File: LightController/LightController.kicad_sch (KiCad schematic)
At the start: 6 parts, among them J1 Conn_01x04_Male, U1 mh-et-live-minikit, U2 TLC59208F, U3 TLC59208F, U4 TLC59208F, U5 TLC59208F

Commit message: routing almost done
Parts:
- removed J1: Conn_01x04_Male, Connector_Phoenix_MC:PhoenixContact_MCV_1,5_4-G-3.5_1x04_P3.50mm_Vertical, symbol Connector:Conn_01x04_Male
- removed U2, U3, U4, U5: TLC59208F, Package_SO:TSSOP-16_4.4x5mm_P0.65mm, symbol bouni:TLC59208F
- added BTN1, BTN2: SW_Push_Open, Button_Switch_SMD:SW_SPST_Omron_B3FS-101xP, symbol Switch:SW_Push_Open
- added D1, D2, D3, D4, D5, D6: LED, LED_SMD:LED_0603_1608Metric, symbol Device:LED
- added F1: Fuse, Fuse:Fuseholder_Cylinder-5x20mm_Schurter_0031_8201_Horizontal_Open, symbol Device:Fuse
- added J0, J1, J2, J3, J4, J5, J6, J7: Conn_01x08_Female, bouni:SPTAF_1_8_3_5_EL, symbol Connector:Conn_01x08_Female
- added J8: Conn_01x02_Female, Connector_Phoenix_MC:PhoenixContact_MC_1,5_2-G-3.5_1x02_P3.50mm_Horizontal, symbol Connector:Conn_01x02_Female
- added JP1: Jumper_2_Open, Jumper:SolderJumper-2_P1.3mm_Open_RoundedPad1.0x1.5mm, symbol Jumper:Jumper_2_Open
- added Q0, Q1, Q10, Q11, Q12, Q13, Q14, Q15, Q16, Q17, Q18, Q19, Q2, Q20, Q21, Q22, Q23, Q24, Q25, Q26, Q27, Q28, Q29, Q3, Q30, Q31, Q32, Q33, Q34, Q35, Q4, Q5, Q6, Q7, Q8, Q9: IRLML0030, Package_TO_SOT_SMD:SOT-23, symbol Transistor_FET:IRLML0030
- added R1: 10K, Resistor_SMD:R_0603_1608Metric, symbol Device:R
- added R2, R3, R4, R5, R6, R7: R, Resistor_SMD:R_0603_1608Metric, symbol Device:R
- added RN1, RN2, RN3, RN4, RN5, RN6, RN7, RN8, RN9: 10k, Resistor_SMD:R_Array_Concave_4x0603, symbol Device:R_Pack04_Split
- added U2, U3: MCP23017_SO, Package_SO:SSOP-28_5.3x10.2mm_P0.65mm, symbol Interface_Expansion:MCP23017_SO
- added U4: D-SUN-MP1584EN, bouni:D-SUN-MP1584EN, symbol bouni:D-SUN-MP1584EN
- added U5: DHT22, Sensor:Aosong_DHT11_5.5x12.0_P2.54mm, symbol Sensor:DHT11
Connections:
- net 5V is gone; now on net +5V: U1.28 (5V)
- net +5V: now also R1.1, R3.2, R4.2, R5.2, R6.2, R7.2, U2.10 (VSS), U3.10 (VSS), U3.15 (A0), U4.7 (VOUT+), U4.8 (VOUT+)
- net GND: now also BTN1.1 (A), BTN2.1 (A), D1.1 (K), D4.1 (K), J8.2 (Pin_2), Q0.3 (D), Q1.3 (D), Q10.3 (D), Q11.3 (D), Q12.3 (D), Q13.3 (D), Q14.3 (D), Q15.3 (D), Q16.3 (D), Q17.3 (D), Q18.3 (D), Q19.3 (D), Q2.3 (D), Q20.3 (D), Q21.3 (D), Q22.3 (D), Q23.3 (D), Q24.3 (D), Q25.3 (D), Q26.3 (D), Q27.3 (D), Q28.3 (D), Q29.3 (D), Q3.3 (D), Q30.3 (D), Q31.3 (D), Q32.3 (D), Q33.3 (D), Q34.3 (D), Q35.3 (D), Q4.3 (D), Q5.3 (D), Q6.3 (D), Q7.3 (D), Q8.3 (D), Q9.3 (D), RN1.5 (R4.2), RN1.6 (R3.2), RN1.7 (R2.2), RN1.8 (R1.2), RN2.5 (R4.2), RN2.6 (R3.2), RN2.7 (R2.2), RN2.8 (R1.2), RN3.5 (R4.2), RN3.6 (R3.2), RN3.7 (R2.2), RN3.8 (R1.2), RN4.5 (R4.2), RN4.6 (R3.2), RN4.7 (R2.2), RN4.8 (R1.2), RN5.5 (R4.2), RN5.6 (R3.2), RN5.7 (R2.2), RN5.8 (R1.2), RN6.5 (R4.2), RN6.6 (R3.2), RN6.7 (R2.2), RN6.8 (R1.2), RN7.5 (R4.2), RN7.6 (R3.2), RN7.7 (R2.2), RN7.8 (R1.2), RN8.5 (R4.2), RN8.6 (R3.2), RN8.7 (R2.2), RN8.8 (R1.2), RN9.5 (R4.2), RN9.6 (R3.2), RN9.7 (R2.2), RN9.8 (R1.2), U2.15 (A0), U2.16 (A1), U2.17 (A2), U2.9 (VDD), U3.16 (A1), U3.17 (A2), U3.9 (VDD), U4.1 (VIN-), U4.2 (VIN-), U4.5 (VOUT-), U4.6 (VOUT-), U5.4 (GND)
- net RESET: now also JP1.1 (A), R1.2, U2.18 (~RESET~), U3.18 (~RESET~)
- net SCL: now also U2.12 (SCK), U3.12 (SCK)
- net SDA: now also U2.13 (SDA), U3.13 (SDA)
- net at U1.11 (RST): now also JP1.2 (B)
- net +3V3: now reaches U1.18 (3V3)
- net +3V3: now also U5.1 (VCC)
- net BTN1: now reaches U1.25 (IO17)
- net BTN1: now also BTN1.2 (B)
- net BTN2: now reaches U1.26 (IO16)
- net BTN2: now also BTN2.2 (B)
- net DHT22: now reaches U1.32 (IO27)
- net DHT22: now also U5.2 (IO)
- net LED1: now reaches U1.33 (IO25)
- net LED1: now also Q32.1 (G), RN9.1 (R1.1)
- net LED2: now reaches U1.34 (IO32)
- net LED2: now also Q33.1 (G), RN9.2 (R2.1)
- net LED3: now reaches U1.35 (TDI)
- net LED3: now also Q34.1 (G), RN9.3 (R3.1)
- net LED4: now reaches U1.36 (IO4)
- net LED4: now also Q35.1 (G), RN9.4 (R4.1)
- new net: D2.1 (K), Q32.2 (S)
- new net: D6.1 (K), Q35.2 (S)
- new net: D6.2 (A), R7.1
- new net: D3.1 (K), Q33.2 (S)
- new net: F1.2, J8.1 (Pin_1)
- new net: D2.2 (A), R3.1
- new net: D3.2 (A), R4.1
- new net: D5.2 (A), R6.1
- new net: D1.2 (A), R2.1
- new net: D4.2 (A), R5.1
- new net: D5.1 (K), Q34.2 (S)
- new net +12V: F1.1, J0.1 (Pin_1), J0.3 (Pin_3), J0.5 (Pin_5), J0.7 (Pin_7), J1.1 (Pin_1), J1.3 (Pin_3), J1.5 (Pin_5), J1.7 (Pin_7), J2.1 (Pin_1), J2.3 (Pin_3), J2.5 (Pin_5), J2.7 (Pin_7), J3.1 (Pin_1), J3.3 (Pin_3), J3.5 (Pin_5), J3.7 (Pin_7), J4.1 (Pin_1), J4.3 (Pin_3), J4.5 (Pin_5), J4.7 (Pin_7), J5.1 (Pin_1), J5.3 (Pin_3), J5.5 (Pin_5), J5.7 (Pin_7), J6.1 (Pin_1), J6.3 (Pin_3), J6.5 (Pin_5), J6.7 (Pin_7), J7.1 (Pin_1), J7.3 (Pin_3), J7.5 (Pin_5), J7.7 (Pin_7), R2.2, U4.3 (VIN+), U4.4 (VIN+)
- new net GPIO0: Q0.1 (G), RN1.1 (R1.1), U2.21 (GPA0)
- new net GPIO1: Q1.1 (G), RN1.2 (R2.1), U2.22 (GPA1)
- new net GPIO10: Q10.1 (G), RN3.3 (R3.1), U2.3 (GPB2)
- new net GPIO11: Q11.1 (G), RN3.4 (R4.1), U2.4 (GPB3)
- new net GPIO12: Q12.1 (G), RN4.1 (R1.1), U2.5 (GPB4)
- new net GPIO13: Q13.1 (G), RN4.2 (R2.1), U2.6 (GPB5)
- new net GPIO14: Q14.1 (G), RN4.3 (R3.1), U2.7 (GPB6)
- new net GPIO15: Q15.1 (G), RN4.4 (R4.1), U2.8 (GPB7)
- new net GPIO16: Q16.1 (G), RN5.1 (R1.1), U3.21 (GPA0)
- new net GPIO17: Q17.1 (G), RN5.2 (R2.1), U3.22 (GPA1)
- new net GPIO18: Q18.1 (G), RN5.3 (R3.1), U3.23 (GPA2)
- new net GPIO19: Q19.1 (G), RN5.4 (R4.1), U3.24 (GPA3)
- new net GPIO2: Q2.1 (G), RN1.3 (R3.1), U2.23 (GPA2)
- new net GPIO20: Q20.1 (G), RN6.1 (R1.1), U3.25 (GPA4)
- new net GPIO21: Q21.1 (G), RN6.2 (R2.1), U3.26 (GPA5)
- new net GPIO22: Q22.1 (G), RN6.3 (R3.1), U3.27 (GPA6)
- new net GPIO23: Q23.1 (G), RN6.4 (R4.1), U3.28 (GPA7)
- new net GPIO24: Q24.1 (G), RN7.1 (R1.1), U3.1 (GPB0)
- new net GPIO25: Q25.1 (G), RN7.2 (R2.1), U3.2 (GPB1)
- new net GPIO26: Q26.1 (G), RN7.3 (R3.1), U3.3 (GPB2)
- new net GPIO27: Q27.1 (G), RN7.4 (R4.1), U3.4 (GPB3)
- new net GPIO28: Q28.1 (G), RN8.1 (R1.1), U3.5 (GPB4)
- new net GPIO29: Q29.1 (G), RN8.2 (R2.1), U3.6 (GPB5)
- new net GPIO3: Q3.1 (G), RN1.4 (R4.1), U2.24 (GPA3)
- new net GPIO30: Q30.1 (G), RN8.3 (R3.1), U3.7 (GPB6)
- new net GPIO31: Q31.1 (G), RN8.4 (R4.1), U3.8 (GPB7)
- new net GPIO4: Q4.1 (G), RN2.1 (R1.1), U2.25 (GPA4)
- new net GPIO5: Q5.1 (G), RN2.2 (R2.1), U2.26 (GPA5)
- new net GPIO6: Q6.1 (G), RN2.3 (R3.1), U2.27 (GPA6)
- new net GPIO7: Q7.1 (G), RN2.4 (R4.1), U2.28 (GPA7)
- new net GPIO8: Q8.1 (G), RN3.1 (R1.1), U2.1 (GPB0)
- new net GPIO9: Q9.1 (G), RN3.2 (R2.1), U2.2 (GPB1)
- new net OUT0: J0.2 (Pin_2), Q0.2 (S)
- new net OUT1: J0.4 (Pin_4), Q1.2 (S)
- new net OUT10: J2.6 (Pin_6), Q10.2 (S)
- new net OUT11: J2.8 (Pin_8), Q11.2 (S)
- new net OUT12: J3.2 (Pin_2), Q12.2 (S)
- new net OUT13: J3.4 (Pin_4), Q13.2 (S)
- new net OUT14: J3.6 (Pin_6), Q14.2 (S)
- new net OUT15: J3.8 (Pin_8), Q15.2 (S)
- new net OUT16: J4.2 (Pin_2), Q16.2 (S)
- new net OUT17: J4.4 (Pin_4), Q17.2 (S)
- new net OUT18: J4.6 (Pin_6), Q18.2 (S)
- new net OUT19: J4.8 (Pin_8), Q19.2 (S)
- new net OUT2: J0.6 (Pin_6), Q2.2 (S)
- new net OUT20: J5.2 (Pin_2), Q20.2 (S)
- new net OUT21: J5.4 (Pin_4), Q21.2 (S)
- new net OUT22: J5.6 (Pin_6), Q22.2 (S)
- new net OUT23: J5.8 (Pin_8), Q23.2 (S)
- new net OUT24: J6.2 (Pin_2), Q24.2 (S)
- new net OUT25: J6.4 (Pin_4), Q25.2 (S)
- new net OUT26: J6.6 (Pin_6), Q26.2 (S)
- new net OUT27: J6.8 (Pin_8), Q27.2 (S)
- new net OUT28: J7.2 (Pin_2), Q28.2 (S)
- new net OUT29: J7.4 (Pin_4), Q29.2 (S)
- new net OUT3: J0.8 (Pin_8), Q3.2 (S)
- new net OUT30: J7.6 (Pin_6), Q30.2 (S)
- new net OUT31: J7.8 (Pin_8), Q31.2 (S)
- new net OUT4: J1.2 (Pin_2), Q4.2 (S)
- new net OUT5: J1.4 (Pin_4), Q5.2 (S)
- new net OUT6: J1.6 (Pin_6), Q6.2 (S)
- new net OUT7: J1.8 (Pin_8), Q7.2 (S)
- new net OUT8: J2.2 (Pin_2), Q8.2 (S)
- new net OUT9: J2.4 (Pin_4), Q9.2 (S)
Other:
- note added: "Connectors: SPTAF 1/ 8-3,5-EL - 1862107"
- note removed: "40h"
- note removed: "42h"
- note removed: "44h"
- note removed: "46h"
- moved on the sheet: U1

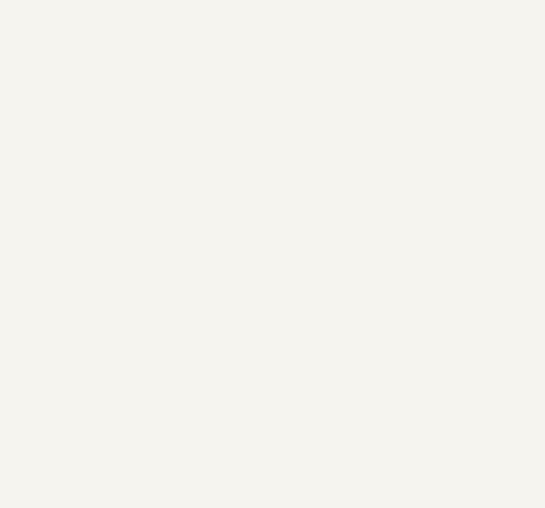
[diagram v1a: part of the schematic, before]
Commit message: made pcb slightly bigger for mounting holes
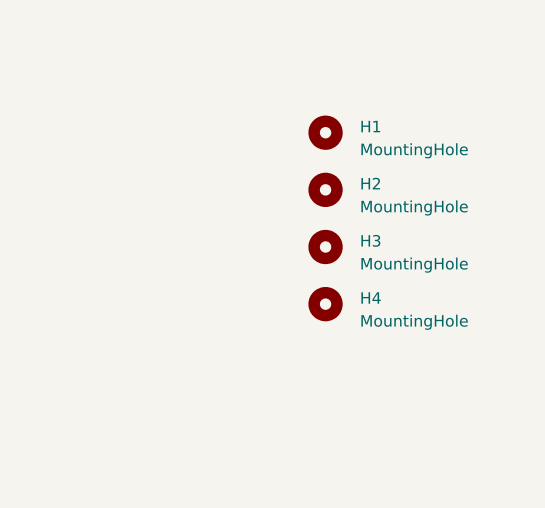
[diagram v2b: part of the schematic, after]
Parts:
- added H1, H2, H3, H4: MountingHole, MountingHole:MountingHole_3.2mm_M3, symbol Mechanical:MountingHole
- J8: footprint Connector_Phoenix_MC:PhoenixContact_MC_1,5_2-G-3.5_1x02_P3.50mm_Horizontal -> bouni:SPTAF_1_2_3_5_EL
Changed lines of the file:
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@@
     (pin "1")
+  )
+  (symbol (lib_id "Mechanical:MountingHole") (at 381 25.4 0) (unit 1)
+    (in_bom yes) (on_board yes)
+    (property "Reference" "H1" (id 0) (at 384.81 24.7649 0)
+      (effects (font (size 1.27 1.27)) (justify left))
+    )
+    (property "Value" "MountingHole" (id 1) (at 384.81 27.3049 0)
+      (effects (font (size 1.27 1.27)) (justify left))
+    )
+    (property "Footprint" "MountingHole:MountingHole_3.2mm_M3" (id 2) (at 381 25.4 0)
+      (effects (font (size 1.27 1.27)) hide)
+    )
+    (property "Datasheet" "~" (id 3) (at 381 25.4 0)
+      (effects (font (size 1.27 1.27)) hide)
+    )
+  )
+  (symbol (lib_id "Mechanical:MountingHole") (at 381 31.75 0) (unit 1)
+    (in_bom yes) (on_board yes)
+    (property "Reference" "H2" (id 0) (at 384.81 31.1149 0)
+      (effects (font (size 1.27 1.27)) (justify left))
+    )
+    (property "Value" "MountingHole" (id 1) (at 384.81 33.6549 0)
+      (effects (font (size 1.27 1.27)) (justify left))
+    )
+    (property "Footprint" "MountingHole:MountingHole_3.2mm_M3" (id 2) (at 381 31.75 0)
+      (effects (font (size 1.27 1.27)) hide)
+    )
+    (property "Datasheet" "~" (id 3) (at 381 31.75 0)
+      (effects (font (size 1.27 1.27)) hide)
+    )
+  )
+  (symbol (lib_id "Mechanical:MountingHole") (at 381 38.1 0) (unit 1)
+    (in_bom yes) (on_board yes)
+    (property "Reference" "H3" (id 0) (at 384.81 37.4649 0)
+      (effects (font (size 1.27 1.27)) (justify left))
+    )
+    (property "Value" "MountingHole" (id 1) (at 384.81 40.0049 0)
+      (effects (font (size 1.27 1.27)) (justify left))
+    )
+    (property "Footprint" "MountingHole:MountingHole_3.2mm_M3" (id 2) (at 381 38.1 0)
+      (effects (font (size 1.27 1.27)) hide)
+    )
+    (property "Datasheet" "~" (id 3) (at 381 38.1 0)
+      (effects (font (size 1.27 1.27)) hide)
+    )
+  )
+  (symbol (lib_id "Mechanical:MountingHole") (at 381 44.45 0) (unit 1)
+    (in_bom yes) (on_board yes)
+    (property "Reference" "H4" (id 0) (at 384.81 43.8149 0)
+      (effects (font (size 1.27 1.27)) (justify left))
+    )
+    (property "Value" "MountingHole" (id 1) (at 384.81 46.3549 0)
+      (effects (font (size 1.27 1.27)) (justify left))
+    )
+    (property "Footprint" "MountingHole:MountingHole_3.2mm_M3" (id 2) (at 381 44.45 0)
+      (effects (font (size 1.27 1.27)) hide)
+    )
+    (property "Datasheet" "~" (id 3) (at 381 44.45 0)
+      (effects (font (size 1.27 1.27)) hide)
+    )
   )
   (symbol (lib_id "Device:Fuse") (at 310.515 150.495 90) (unit 1)
@@
       (effects (font (size 1.27 1.27)) (justify left) hide)
     )
-    (property "Footprint" "Connector_Phoenix_MC:PhoenixContact_MC_1,5_2-G-3.5_1x02_P3.50mm_Horizontal" (id 2) (at 320.675 150.495 0)
+    (property "Footprint" "bouni:SPTAF_1_2_3_5_EL" (id 2) (at 320.675 150.495 0)
       (effects (font (size 1.27 1.27)) hide)
     )
@@
       (reference "F1") (unit 1) (value "Fuse") (footprint "Fuse:Fuseholder_Cylinder-5x20mm_Schurter_0031_8201_Horizontal_Open")
     )
+    (path "/0e0db03e-b571-4352-b777-45bc72d96060"
+      (reference "H1") (unit 1) (value "MountingHole") (footprint "MountingHole:MountingHole_3.2mm_M3")
+    )
+    (path "/4b637edb-9f0e-4f96-bd27-e5f48b42a3f5"
+      (reference "H2") (unit 1) (value "MountingHole") (footprint "MountingHole:MountingHole_3.2mm_M3")
+    )
+    (path "/6c0fcb80-8a01-42df-9250-fdfbdc127efc"
+      (reference "H3") (unit 1) (value "MountingHole") (footprint "MountingHole:MountingHole_3.2mm_M3")
+    )
+    (path "/79dee40a-cfc9-42e3-bafe-178bb33cb5f9"
+      (reference "H4") (unit 1) (value "MountingHole") (footprint "MountingHole:MountingHole_3.2mm_M3")
+    )
     (path "/4fcb31af-0770-4aa7-a292-8703c88905c7"
       (reference "J0") (unit 1) (value "Conn_01x08_Female") (footprint "bouni:SPTAF_1_8_3_5_EL")
@@
     )
     (path "/2e2b9d4e-e6e7-44fa-a680-4714323d8b5f"
-      (reference "J8") (unit 1) (value "Conn_01x02_Female") (footprint "Connector_Phoenix_MC:PhoenixContact_MC_1,5_2-G-3.5_1x02_P3.50mm_Horizontal")
+      (reference "J8") (unit 1) (value "Conn_01x02_Female") (footprint "bouni:SPTAF_1_2_3_5_EL")
     )
     (path "/18081312-65bd-47db-861b-dcfb9690463b"

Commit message: started positioning labels
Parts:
- added H5, H6: MountingHole, MountingHole:MountingHole_3.2mm_M3, symbol Mechanical:MountingHole
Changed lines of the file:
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@@
+    )
+  )
+  (symbol (lib_id "Mechanical:MountingHole") (at 381 50.8 0) (unit 1)
+    (in_bom yes) (on_board yes)
+    (property "Reference" "H5" (id 0) (at 384.81 50.1649 0)
+      (effects (font (size 1.27 1.27)) (justify left))
+    )
+    (property "Value" "MountingHole" (id 1) (at 384.81 52.7049 0)
+      (effects (font (size 1.27 1.27)) (justify left))
+    )
+    (property "Footprint" "MountingHole:MountingHole_3.2mm_M3" (id 2) (at 381 50.8 0)
+      (effects (font (size 1.27 1.27)) hide)
+    )
+    (property "Datasheet" "~" (id 3) (at 381 50.8 0)
+      (effects (font (size 1.27 1.27)) hide)
+    )
+  )
+  (symbol (lib_id "Mechanical:MountingHole") (at 381 57.15 0) (unit 1)
+    (in_bom yes) (on_board yes)
+    (property "Reference" "H6" (id 0) (at 384.81 56.5149 0)
+      (effects (font (size 1.27 1.27)) (justify left))
+    )
+    (property "Value" "MountingHole" (id 1) (at 384.81 59.0549 0)
+      (effects (font (size 1.27 1.27)) (justify left))
+    )
+    (property "Footprint" "MountingHole:MountingHole_3.2mm_M3" (id 2) (at 381 57.15 0)
+      (effects (font (size 1.27 1.27)) hide)
+    )
+    (property "Datasheet" "~" (id 3) (at 381 57.15 0)
+      (effects (font (size 1.27 1.27)) hide)
     )
   )
@@
       (reference "H4") (unit 1) (value "MountingHole") (footprint "MountingHole:MountingHole_3.2mm_M3")
     )
+    (path "/b4b498a6-a5fc-4fad-a424-99df459242cf"
+      (reference "H5") (unit 1) (value "MountingHole") (footprint "MountingHole:MountingHole_3.2mm_M3")
+    )
+    (path "/21d4f7fe-e028-4097-9cee-0fa58146e09d"
+      (reference "H6") (unit 1) (value "MountingHole") (footprint "MountingHole:MountingHole_3.2mm_M3")
+    )
     (path "/4fcb31af-0770-4aa7-a292-8703c88905c7"
